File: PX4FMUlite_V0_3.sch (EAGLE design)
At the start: 146 parts, among them J2 DF13-4P-1.25V, J201 DF13C-6P-1.25V, J202 DF13C-6P-1.25V, J203 DF13C-6P-1.25V, J3 DF13C-4P-1.25V, J302 DF13C-4P-1.25V, J401 DF13C-4P-1.25V, J403 DF13C-7P-1.25V, J405 DF13C-4P-1.25V, J801 JST-ZH-3, J802 DF13C-3P-1.25V, M3_MOUNT1101 MOUNT-HOLE3.1MM, M3_MOUNT1102 MOUNT-HOLE3.1MM, M3_MOUNT1103 MOUNT-HOLE3.1MM, M3_MOUNT1104 MOUNT-HOLE3.1MM, U101 STM32F4X7VX, U2 MAX3051, U401 MAX3051, U903 74LVC2G240, X101 3.2x2.5 mm / 24 MHz / 15 ppm

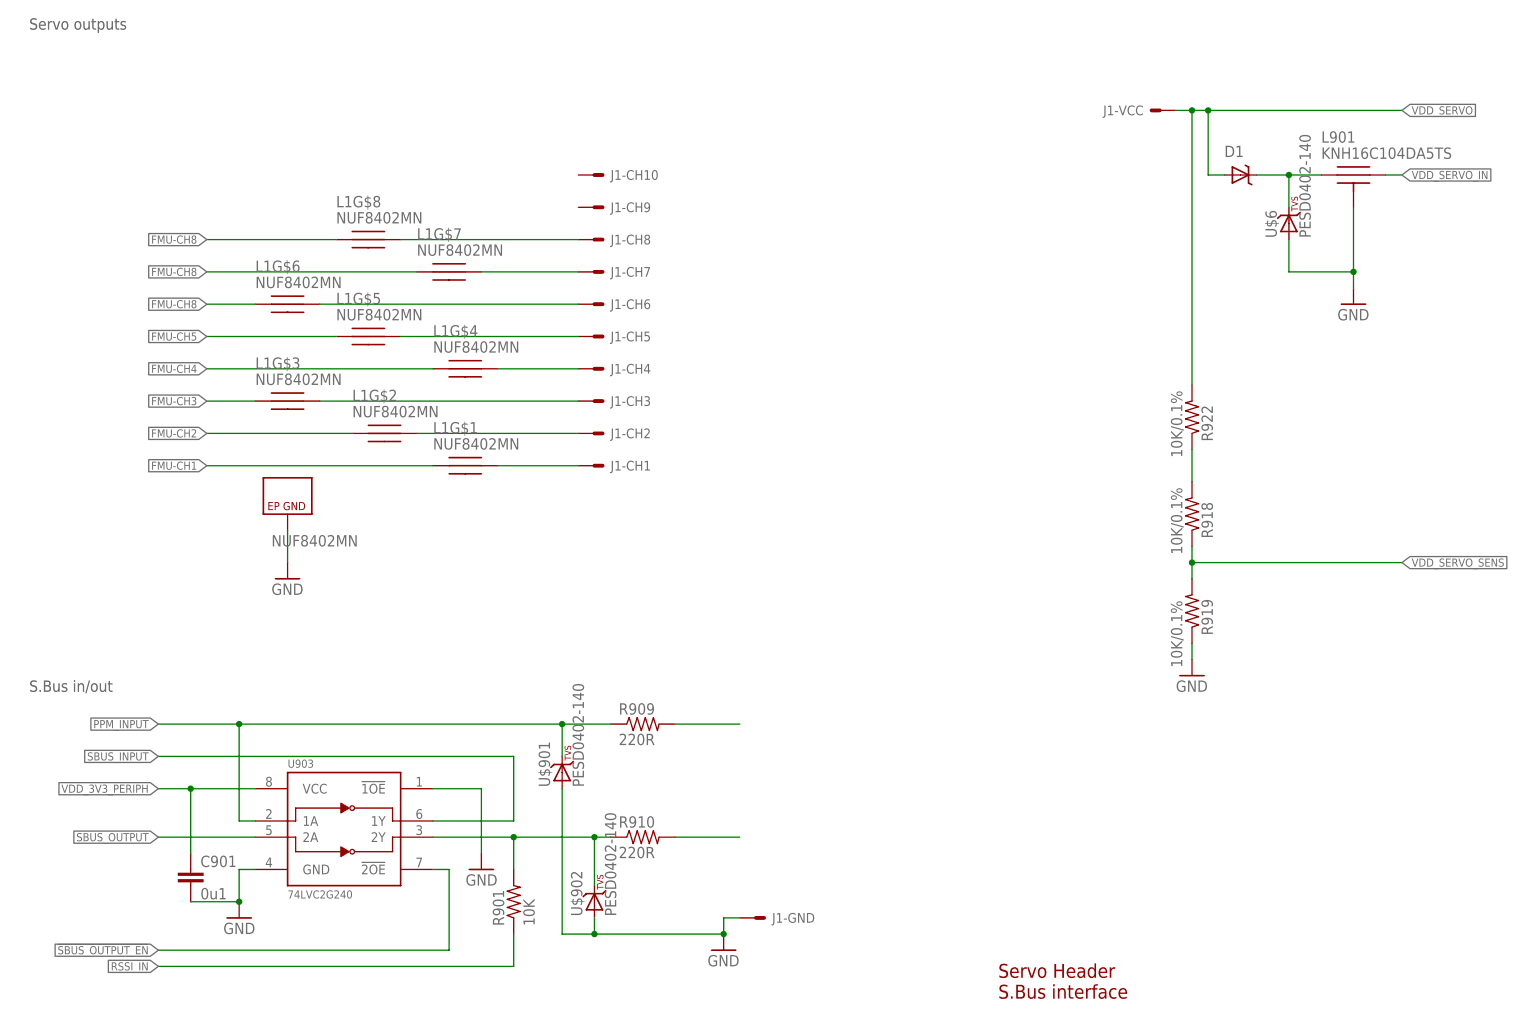
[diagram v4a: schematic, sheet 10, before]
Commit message: Added power input diodes
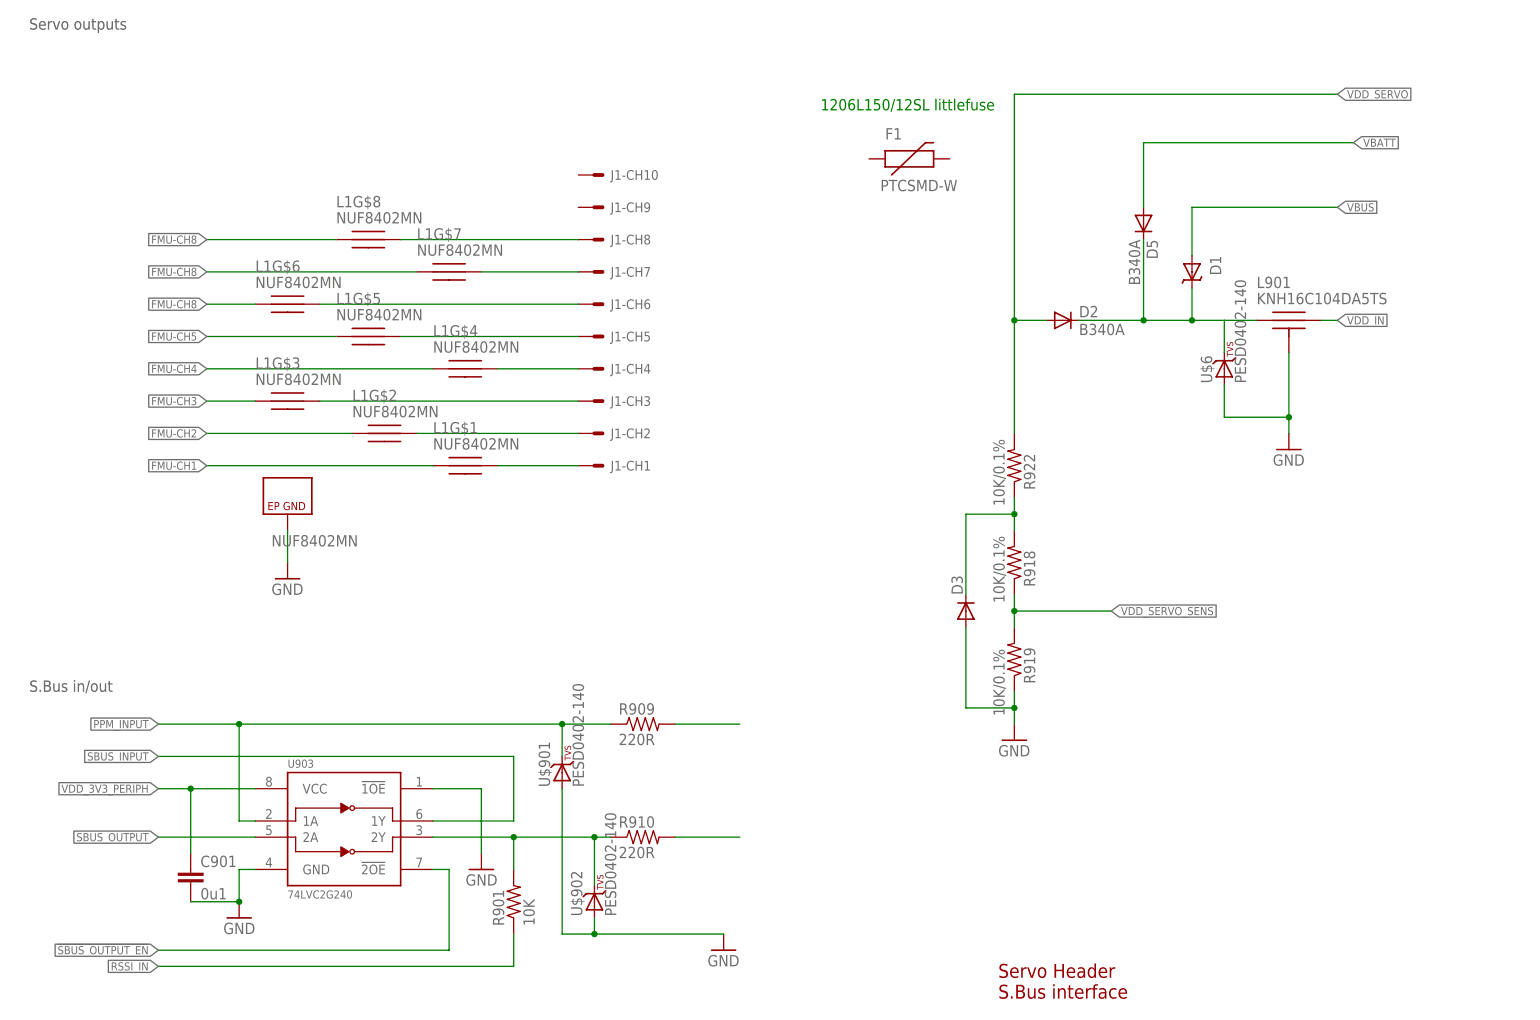
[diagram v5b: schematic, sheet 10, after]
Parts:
- added D2, D5: B340A, SparkFun-DiscreteSemi:DIODESMA
- added D3: (no value), SparkFun-DiscreteSemi:DIODESOD
- added F1: PTCSMD-W, SparkFun-PowerIC:PTCSMD-W
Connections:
- net VDD_SERVO_IN renamed VDD_IN
- removed net GNDX: C1001.2, C1002.2, C1003.2, C1004.2, C102.2, C103.1, C2.2, C3.2, C4.2, C402.2, C5.2, C505.2, C506.2, C508.2, C601.2, C602.1, C603.2, C604.2, C605.2, C606.2, C607.2, C608.2, C609.1, C610.2, C611.2, C612.2, C613.2, C901.2, GND..P$1, GND.P$1, J1-GND.S, J201.6, J202.6, J203.6, J3.4, J302.4, J401.4, J403.7, J405.4, J801.P$2, JX301-GND1.S, JX301-GND2.S, JX301-GND3.S, JX801.GND, L201.P$3, L202.P$3, L203.P$3, L4.P$3, L402.P$3, L403.P$3, L603.P$3, L7.P$3, L901.P$3, R1002.1, R102.2, R5.1, R606.2, R607.2, R610.2, R611.1, R711.1, R713.2, R919.1, S601.2, U$1.3, U$1002.GND, U$2.GND, U$2.RSV1, U$201.A, U$202.A, U$203.A, U$401.A, U$402.A, U$404.A, U$5.GND, U$6.A, U$604.VBAT, U$604.VSS, U$605.GND, U$7.A, U$701.A, U$801.A, U$901.A, U$902.A, U101BAT.VSSA, U101G$2.VSS, U2.GND, U2.RS, U2.SHDN, U401.GND, U401.RS, U401.SHDN, U903.!1OE, U903.GND, X101.NC_2, X101.NC_4
- removed net N$110: D1.C, L901.P$1, U$6.C
- new net N$6: D3.C, R918.2, R922.1
- new net VBATT: D5.A
- net GND: now also C1001.2, C1002.2, C1003.2, C1004.2, C102.2, C103.1, C2.2, C3.2, C4.2, C402.2, C5.2, C505.2, C506.2, C508.2, C601.2, C602.1, C603.2, C604.2, C605.2, C606.2, C607.2, C608.2, C609.1, C610.2, C611.2, C612.2, C613.2, C901.2, D3.A, GND..P$1, GND.P$1, J201.6, J202.6, J203.6, J3.4, J302.4, J401.4, J403.7, J405.4, J801.P$2, JX301-GND1.S, JX301-GND2.S, JX301-GND3.S, JX801.GND, L201.P$3, L202.P$3, L203.P$3, L4.P$3, L402.P$3, L403.P$3, L603.P$3, L7.P$3, L901.P$3, R1002.1, R102.2, R5.1, R606.2, R607.2, R610.2, R611.1, R711.1, R713.2, R919.1, S601.2, U$1.3, U$1002.GND, U$2.GND, U$2.RSV1, U$201.A, U$202.A, U$203.A, U$401.A, U$402.A, U$404.A, U$5.GND, U$6.A, U$604.VBAT, U$604.VSS, U$605.GND, U$7.A, U$701.A, U$801.A, U$901.A, U$902.A, U101BAT.VSSA, U101G$2.VSS, U2.GND, U2.RS, U2.SHDN, U401.GND, U401.RS, U401.SHDN, U903.!1OE, U903.GND, X101.NC_2, X101.NC_4
- net N$3: now also D1.C, D2.C, D5.C, L901.P$1, U$6.C; no longer R918.2, R922.1
- net VBUS: now also D1.A
- net VDD_SERVO: now also D2.A; no longer D1.A, J1-VCC.S
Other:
- note added: "1206L150/12SL littlefuse"
- note removed: "PROTECT THIS VDD OUT"
- moved on the sheet: D1, L901, R918, R919, R922, U$6

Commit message: Stuff
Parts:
- removed JX801: HEADER-3X1BOARDEDGE-SHORT, pixhawk2:HEADER-3X1BOARDEDGE-SHORT
- added JP4: JUMPER-3SMD, SparkFun-Passives:JUMPER-3SMD
- added U$14: HEADER-3X1RA, PX4lite:HEADER-3X1RA
- J1: device PX4lite:HEADER-3X10 -> PX4lite:SERVO_HEADER-3X8
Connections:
- net FMU-CH1-PROT: now also J1-CH8.S; no longer J1-CH1.S
- net GND: now also J1-GND.S; no longer JX801.GND
- net IO-USART1_RX: no longer JX801.+5V
- net IO-USART1_TX: no longer JX801.PPM
- net N$15: now also J1-CH1.S; no longer J1-CH8.S
- net N$16: now also J1-CH2.S; no longer J1-CH7.S
- net N$36: now also J1-CH3.S; no longer J1-CH6.S
- net N$68: now also J1-CH4.S; no longer J1-CH5.S
- net N$77: now also J1-CH5.S; no longer J1-CH4.S
- net N$78: now also J1-CH6.S; no longer J1-CH3.S
- net N$79: now also J1-CH7.S; no longer J1-CH2.S
- net VDD_SERVO: now also J1-VCC.S
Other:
- note removed: "IO_SERIAL1"
- moved on the sheet: J1-CH1, J1-CH2, J1-CH3, J1-CH4, J1-CH5, J1-CH6, J1-CH7, J1-CH8, J801, U$801

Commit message: Added cap to TPS63031 buck-boost
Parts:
- removed U$10: GRM21BR61C106KE15L, ti_tps_soln2:GRM21BR61C106KE15L
- removed U$11: GRM155R61C223KA01D, ti_tps_soln2:GRM155R61C223KA01D
- removed U$12: XFL4020-222MEB, ti_tps_soln2:XFL4020-222MEB
- removed U$13: LMK212BJ226MG-T, ti_tps_soln2:LMK212BJ226MG-T
- removed U$8: TPS62143RGTR, ti_tps_soln2:TPS62143RGTR
- removed U$9: CRCW0402100KFKED, ti_tps_soln2:CRCW0402100KFKED
- added C1, C10, C8, C9: 22uF, SparkFun-Capacitors:22UF-16V-20%-(1210)
- added C7: 8p, pixhawk2:CAP0402
- added U$15: TPS6303X, PX4lite:TPS6303X
- added U$16: XFL4020-222MEB, ti_tps_soln2:XFL4020-222MEB
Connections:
- removed net N$40: U$11.1, U$8.SS/TR
- new net N$10: U$15.L2, U$16.1
- new net N$17: U$15.L1, U$16.2
- new net VOUT: C10.1, C8.1, C9.1, U$15.VOUT
- net !VDD_SERVO_VALID: no longer U$8.PG, U$9.2
- net GND: now also U$15.GND; no longer U$10.2, U$11.2, U$13.1, U$8.AGND, U$8.DEF, U$8.ETPAD, U$8.FB, U$8.FSW, U$8.PGND_2
- net N$14: now also C1.2, C10.2, C8.2, C9.2, U$15.PGND; no longer U$12.2, U$8.SW_2
- net VDD_5V_IN: no longer U$12.1, U$13.2, U$8.VOS, U$9.1
- net VDD_IN: now also C1.1, U$15.EN, U$15.VIN; no longer U$10.1, U$8.AVIN, U$8.EN, U$8.PVIN_2

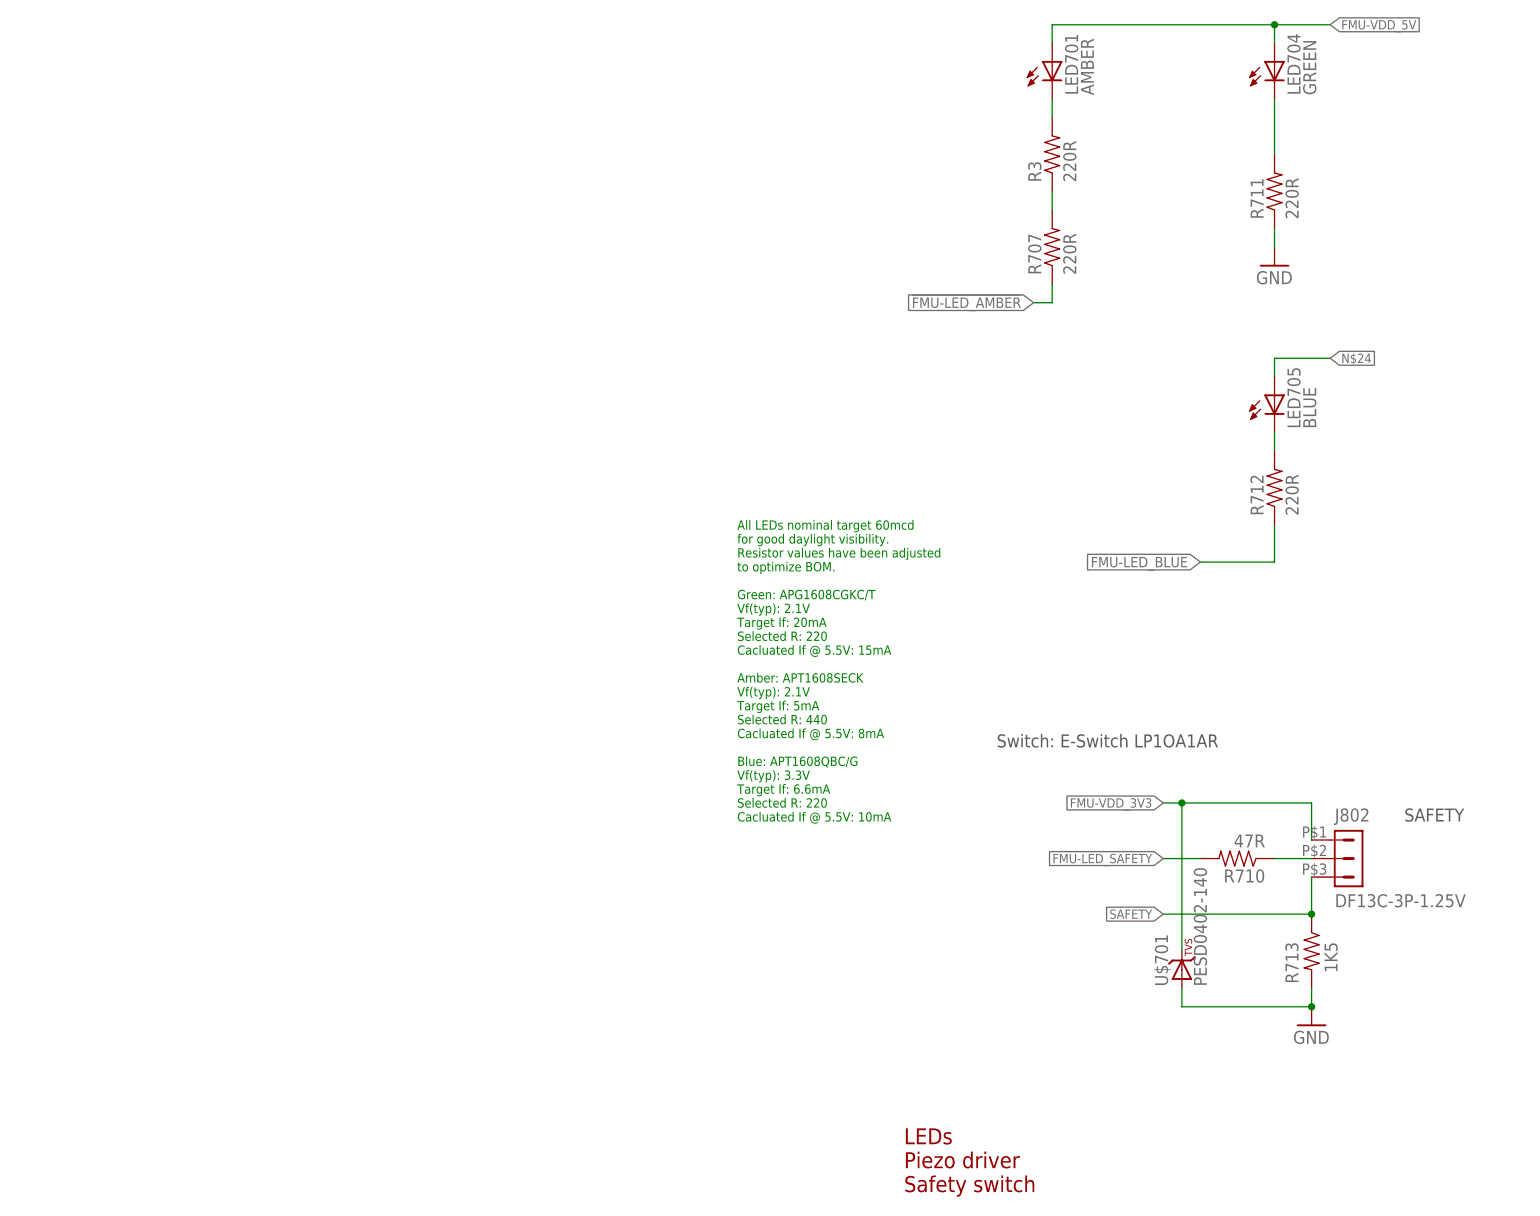
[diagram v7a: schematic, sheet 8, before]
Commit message: Crystal rewire
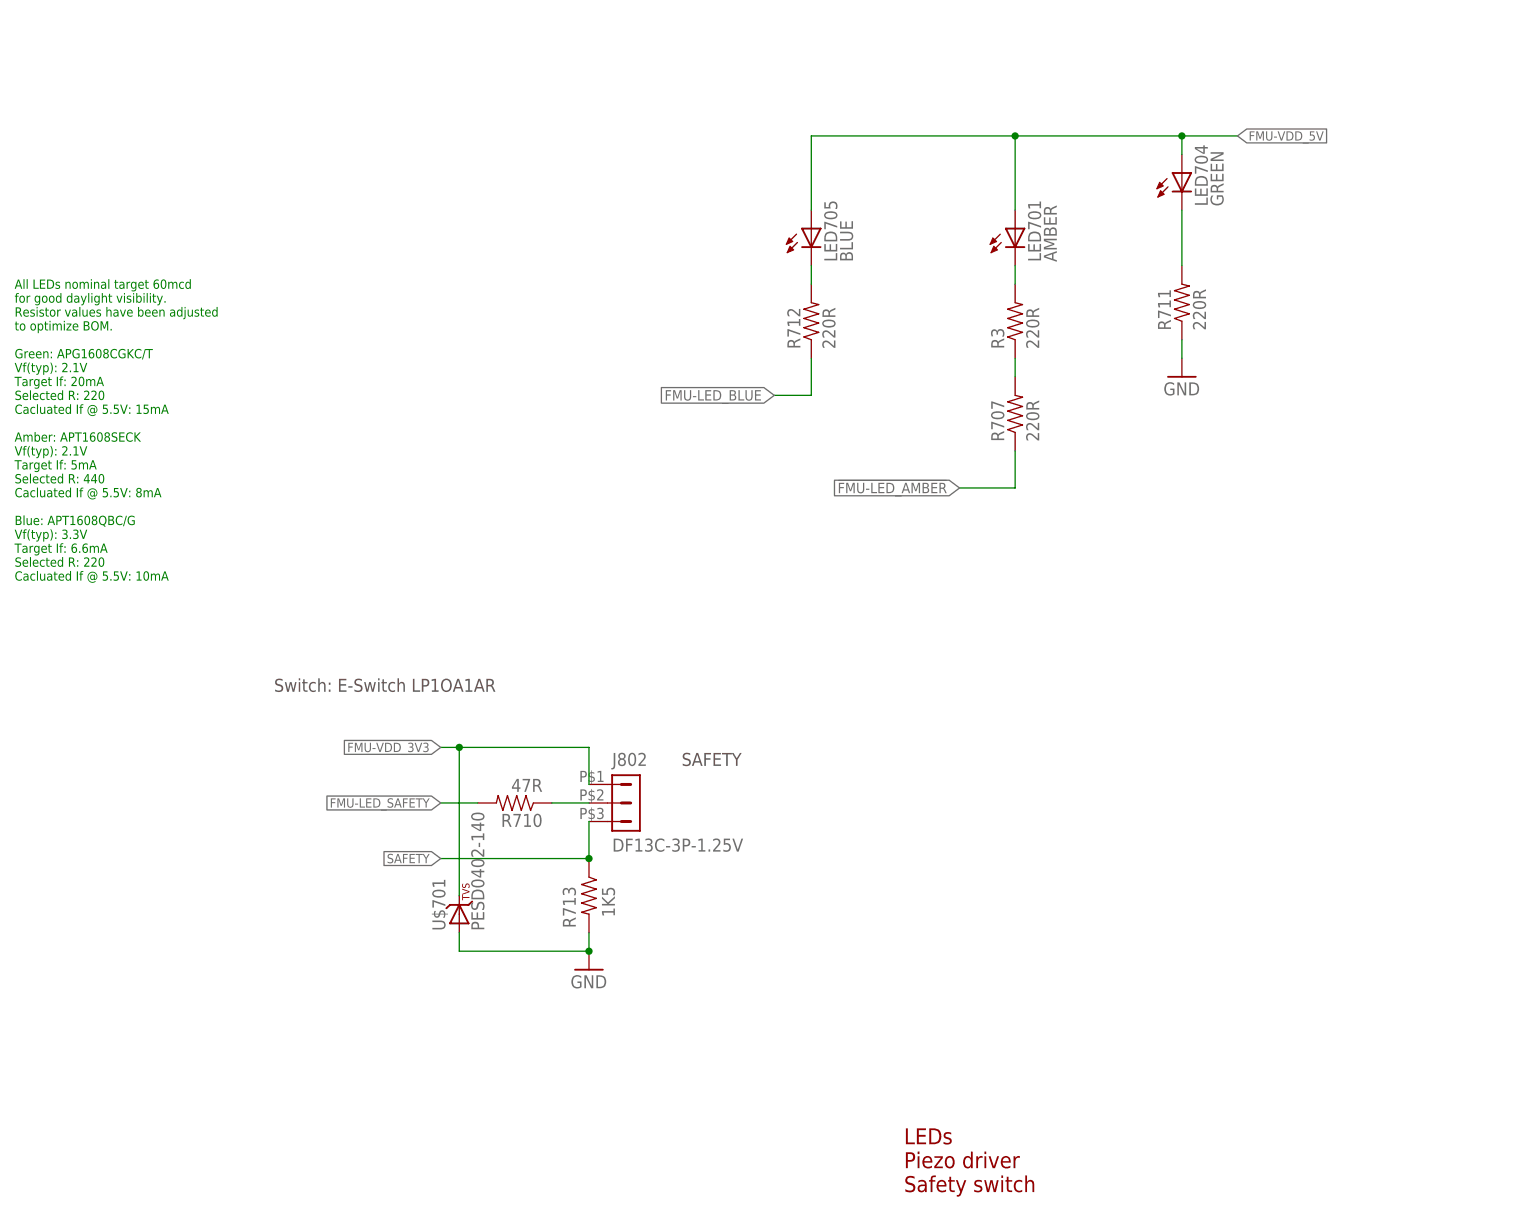
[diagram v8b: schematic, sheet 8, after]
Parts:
- removed F1: PTCSMD-W, SparkFun-PowerIC:PTCSMD-W
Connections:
- removed net N$24: LED705.A
- net FMU-VDD_5V: now also LED705.A
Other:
- moved on the sheet: J1-GND, J802, JP4, LED701, LED704, LED705, R3, R707, R710, R711, R712, R713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
